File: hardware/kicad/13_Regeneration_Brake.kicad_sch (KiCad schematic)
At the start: 25 parts, among them Q1 2N7002, Q2 2N7002, Q3 2N7002, U14 SN74LVC2G04DCKR, U19 TLV9001IDBVR

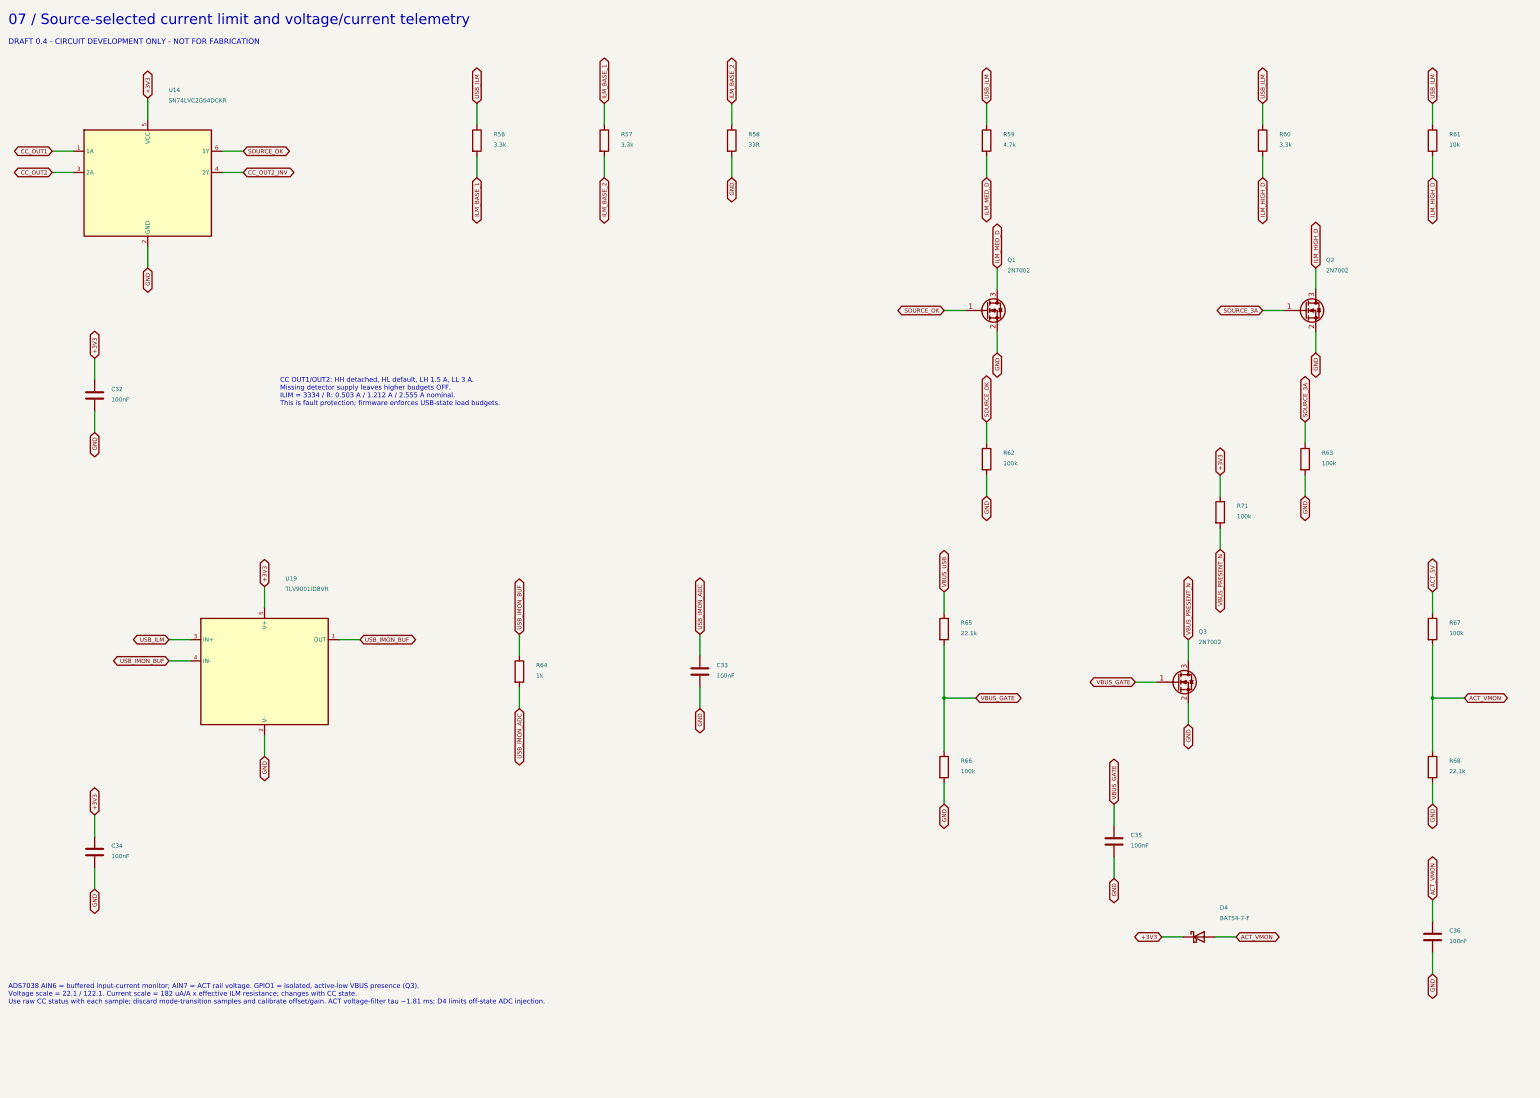
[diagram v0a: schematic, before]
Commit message: Add wheel control circuitry and autonomous regeneration brake
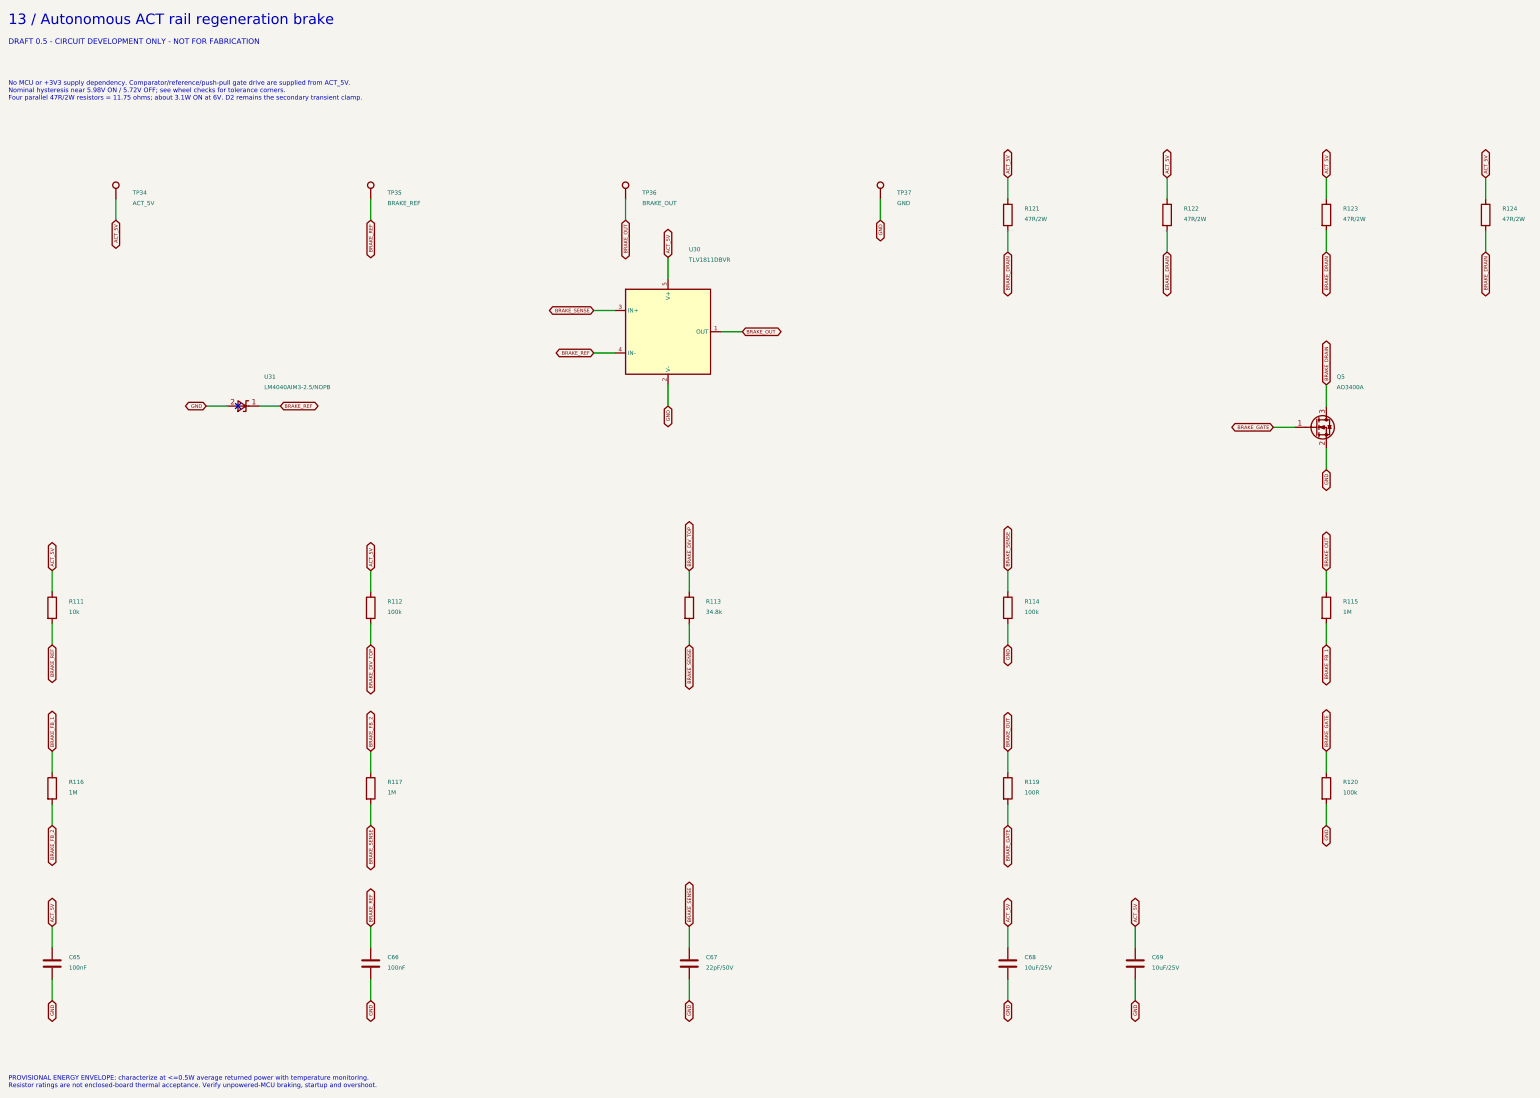
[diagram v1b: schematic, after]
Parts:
- removed C32, C33, C34, C35, C36: 100nF, Capacitor_SMD:C_0603_1608Metric, symbol Device:C
- removed D4: BAT54-7-F, Package_TO_SOT_SMD:SOT-23, symbol MagMouse:BAT54_7_F
- removed Q1, Q2, Q3: 2N7002, Package_TO_SOT_SMD:SOT-23, symbol Transistor_FET:2N7002
- removed R56, R57, R60: 3.3k, Resistor_SMD:R_0603_1608Metric, symbol Device:R
- removed R58: 33R, Resistor_SMD:R_0603_1608Metric, symbol Device:R
- removed R59: 4.7k, Resistor_SMD:R_0603_1608Metric, symbol Device:R
- removed R61: 10k, Resistor_SMD:R_0603_1608Metric, symbol Device:R
- removed R62, R63, R66, R67, R71: 100k, Resistor_SMD:R_0603_1608Metric, symbol Device:R
- removed R64: 1k, Resistor_SMD:R_0603_1608Metric, symbol Device:R
- removed R65, R68: 22.1k, Resistor_SMD:R_0603_1608Metric, symbol Device:R
- removed U14: SN74LVC2G04DCKR, Package_TO_SOT_SMD:SOT-363_SC-70-6, symbol MagMouse:SN74LVC2G04DCKR
- removed U19: TLV9001IDBVR, Package_TO_SOT_SMD:SOT-23-5, symbol MagMouse:TLV9001IDBVR
- added C65, C66: 100nF, Capacitor_SMD:C_0603_1608Metric, symbol Device:C
- added C67: 22pF/50V, Capacitor_SMD:C_0603_1608Metric, symbol Device:C
- added C68, C69: 10uF/25V, Capacitor_SMD:C_0805_2012Metric, symbol Device:C
- added Q5: AO3400A, Package_TO_SOT_SMD:SOT-23, symbol Transistor_FET:AO3400A
- added R111: 10k, Resistor_SMD:R_0603_1608Metric, symbol Device:R
- added R112, R114, R120: 100k, Resistor_SMD:R_0603_1608Metric, symbol Device:R
- added R113: 34.8k, Resistor_SMD:R_0603_1608Metric, symbol Device:R
- added R115, R116, R117: 1M, Resistor_SMD:R_0603_1608Metric, symbol Device:R
- added R119: 100R, Resistor_SMD:R_0603_1608Metric, symbol Device:R
- added R121, R122, R123, R124: 47R/2W, Resistor_SMD:R_2512_6332Metric, symbol Device:R
- added TP34: ACT_5V, TestPoint:TestPoint_Pad_D1.0mm, symbol Connector:TestPoint
- added TP35: BRAKE_REF, TestPoint:TestPoint_Pad_D1.0mm, symbol Connector:TestPoint
- added TP36: BRAKE_OUT, TestPoint:TestPoint_Pad_D1.0mm, symbol Connector:TestPoint
- added TP37: GND, TestPoint:TestPoint_Pad_D1.0mm, symbol Connector:TestPoint
- added U30: TLV1811DBVR, Package_TO_SOT_SMD:SOT-23-5, symbol MagMouse:TLV1811DBVR
- added U31: LM4040AIM3-2.5/NOPB, Package_TO_SOT_SMD:SOT-23, symbol Reference_Voltage:LM4040DBZ-2.5
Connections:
- net ACT_5V: now also C65.1, C68.1, C69.1, R111.1, R112.1, R121.1, R122.1, R123.1, R124.1, TP34.1, U30.5 (V+)
- net GND: now also C65.2, C66.2, C67.2, C68.2, C69.2, Q5.2 (S), R114.2, R120.2, TP37.1, U30.2 (V-), U31.2 (A)
- new net BRAKE_DIV_TOP: R112.2, R113.1
- new net BRAKE_DRAIN: Q5.3 (D), R121.2, R122.2, R123.2, R124.2
- new net BRAKE_FB_1: R115.2, R116.1
- new net BRAKE_FB_2: R116.2, R117.1
- new net BRAKE_GATE: Q5.1 (G), R119.2, R120.1
- new net BRAKE_OUT: R115.1, R119.1, TP36.1, U30.1 (OUT)
- new net BRAKE_REF: C66.1, R111.2, TP35.1, U30.4 (IN-), U31.1 (K)
- new net BRAKE_SENSE: C67.1, R113.2, R114.1, R117.2, U30.3 (IN+)
- no-connect marks 0 -> 1
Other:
- note added: "13 / Autonomous ACT rail regeneration brake"
- note added: "DRAFT 0.5 - CIRCUIT DEVELOPMENT ONLY - NOT FOR FABRICATION"
- note added: "No MCU or +3V3 supply dependency. Comparator/reference/push-pull gate drive are supplied from ACT_5V. Nominal hysteresis near 5.98V ON / 5.72V OFF; see wheel checks for tolerance corners. Four parallel 47R/2W resistors = 11.75 ohms; about 3.1W ON at 6V. D2 remains the secondary transient clamp."
- note added: "PROVISIONAL ENERGY ENVELOPE: characterize at <=0.5W average returned power with temperature monitoring. Resistor ratings are not enclosed-board thermal acceptance. Verify unpowered-MCU braking, startup and overshoot."
- note removed: "07 / Source-selected current limit and voltage/current telemetry"
- note removed: "ADS7038 AIN6 = buffered input-current monitor; AIN7 = ACT rail voltage. GPIO1 = isolated, active-low VBUS presence (Q3). Voltage scale = 22.1 / 122.1. Current scale = 182 uA/A x effective ILM resistance; changes with CC state. Use raw CC status with each sample; discard mode-transition samples and calibrate offset/gain. ACT voltage-filter tau ~1.81 ms; D4 limits off-state ADC injection."
- note removed: "CC OUT1/OUT2: HH detached, HL default, LH 1.5 A, LL 3 A. Missing detector supply leaves higher budgets OFF. ILIM = 3334 / R: 0.503 A / 1.212 A / 2.555 A nominal. This is fault protection; firmware enforces USB-state load budgets."
- note removed: "DRAFT 0.4 - CIRCUIT DEVELOPMENT ONLY - NOT FOR FABRICATION"
- title: MagMouse - 07_Power_Monitor -> MagMouse - 13_Regeneration_Brake
